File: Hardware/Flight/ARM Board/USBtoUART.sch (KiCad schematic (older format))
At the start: 11 parts

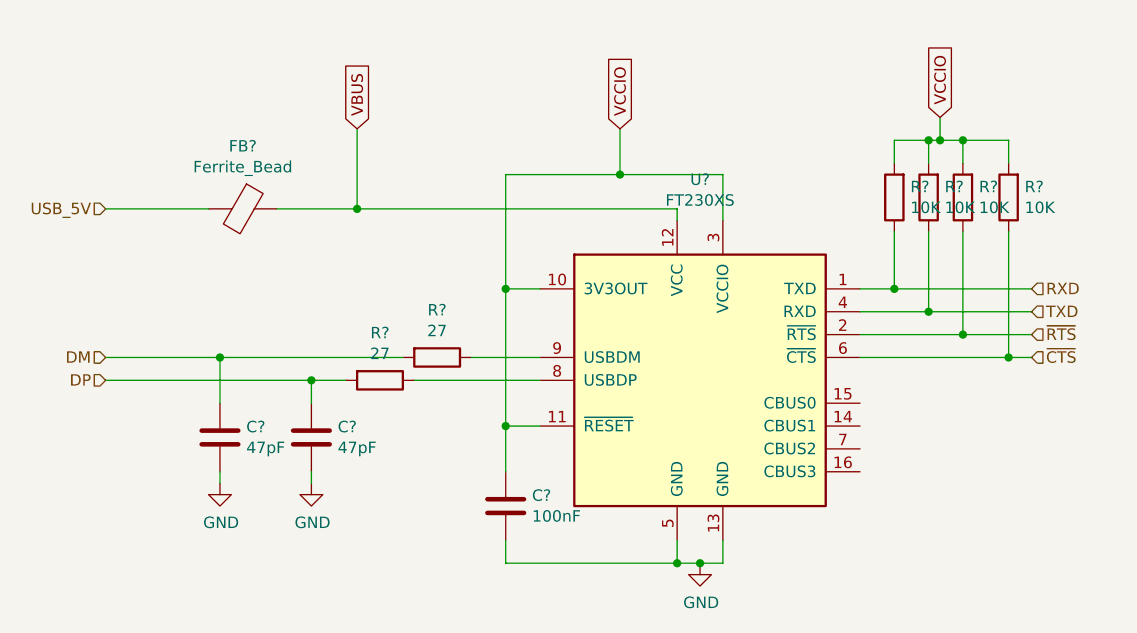
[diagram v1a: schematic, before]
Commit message: Added JTAG I/O, USB UART connections, modified headers and power circuit, added I2C for MSP430
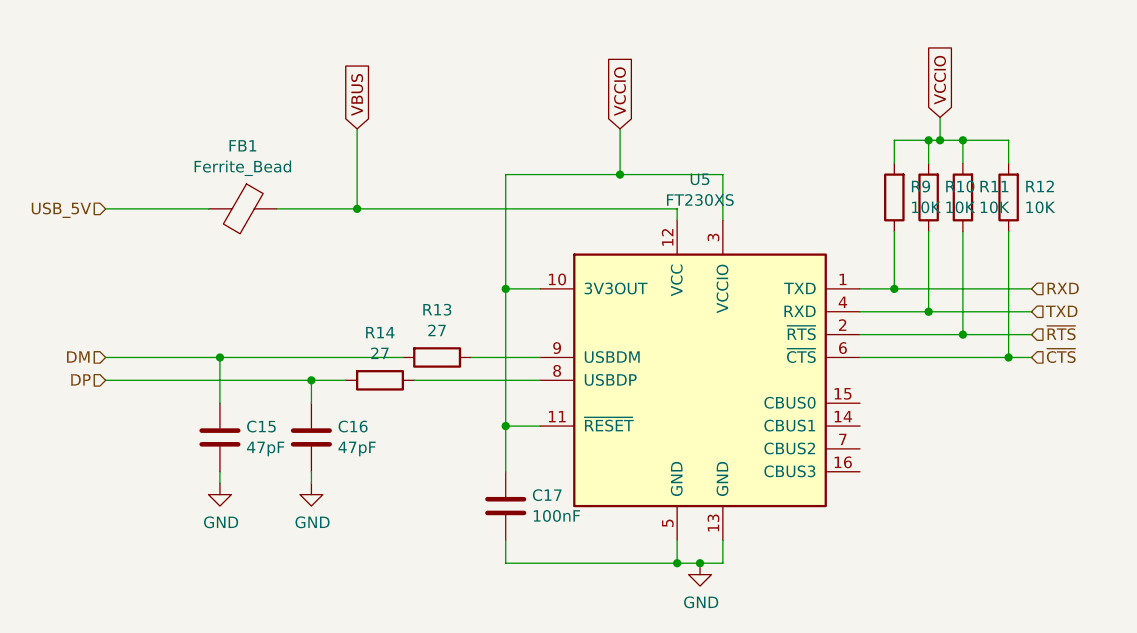
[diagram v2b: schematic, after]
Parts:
- C15, C16: renamed from C?; footprint (none) -> Capacitors_SMD:C_0603
- FB1: renamed from FB?; footprint (none) -> Capacitors_SMD:C_0603
- R10, R11, R12, R13, R14, R9: renamed from R?; footprint (none) -> Resistors_SMD:R_0603
- U5: renamed from U?; footprint Package_SO:SSOP-16_3.9x4.9mm_P0.635mm -> Housings_SSOP:SSOP-16_3.9x4.9mm_Pitch0.635mm
- gave numbers to parts that had none: 1
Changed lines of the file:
@@
 EESchema Schematic File Version 4
+LIBS:ARM Board-cache
 EELAYER 26 0
 EELAYER END
@@
 P 6550 3500
 AR Path="/5C08A0F3" Ref="U?"  Part="1"
-AR Path="/5C089FB0/5C08A0F3" Ref="U?"  Part="1"
-F 0 "U?" H 6550 4378 50  0000 C CNN
+AR Path="/5C089FB0/5C08A0F3" Ref="U5"  Part="1"
+F 0 "U5" H 6550 4378 50  0000 C CNN
 F 1 "FT230XS" H 6550 4287 50  0000 C CNN
-F 2 "Package_SO:SSOP-16_3.9x4.9mm_P0.635mm" H 7000 2850 50  0001 C CNN
+F 2 "Housings_SSOP:SSOP-16_3.9x4.9mm_Pitch0.635mm" H 7000 2850 50  0001 C CNN
 F 3 "http://www.ftdichip.com/Products/ICs/FT230X.html" H 6550 3500 50  0001 C CNN
 	1    6550 3500
@@
 P 4850 3750
 AR Path="/5C08A0FA" Ref="C?"  Part="1"
-AR Path="/5C089FB0/5C08A0FA" Ref="C?"  Part="1"
-F 0 "C?" H 4965 3796 50  0000 L CNN
+AR Path="/5C089FB0/5C08A0FA" Ref="C16"  Part="1"
+F 0 "C16" H 4965 3796 50  0000 L CNN
 F 1 "47pF" H 4965 3705 50  0000 L CNN
-F 2 "" H 4888 3600 50  0001 C CNN
+F 2 "Capacitors_SMD:C_0603" H 4888 3600 50  0001 C CNN
 F 3 "47pF" H 4850 3750 50  0001 C CNN
 	1    4850 3750
@@
 P 4450 3750
 AR Path="/5C08A101" Ref="C?"  Part="1"
-AR Path="/5C089FB0/5C08A101" Ref="C?"  Part="1"
-F 0 "C?" H 4565 3796 50  0000 L CNN
+AR Path="/5C089FB0/5C08A101" Ref="C15"  Part="1"
+F 0 "C15" H 4565 3796 50  0000 L CNN
 F 1 "47pF" H 4565 3705 50  0000 L CNN
-F 2 "" H 4488 3600 50  0001 C CNN
+F 2 "Capacitors_SMD:C_0603" H 4488 3600 50  0001 C CNN
 F 3 "47pF" H 4450 3750 50  0001 C CNN
 	1    4450 3750
@@
 P 5400 3400
 AR Path="/5C08A108" Ref="R?"  Part="1"
-AR Path="/5C089FB0/5C08A108" Ref="R?"  Part="1"
-F 0 "R?" V 5193 3400 50  0000 C CNN
+AR Path="/5C089FB0/5C08A108" Ref="R13"  Part="1"
+F 0 "R13" V 5193 3400 50  0000 C CNN
 F 1 "27" V 5284 3400 50  0000 C CNN
-F 2 "" V 5330 3400 50  0001 C CNN
+F 2 "Resistors_SMD:R_0603" V 5330 3400 50  0001 C CNN
 F 3 "~" H 5400 3400 50  0001 C CNN
 	1    5400 3400
@@
 P 5150 3500
 AR Path="/5C08A10F" Ref="R?"  Part="1"
-AR Path="/5C089FB0/5C08A10F" Ref="R?"  Part="1"
-F 0 "R?" V 4943 3500 50  0000 C CNN
+AR Path="/5C089FB0/5C08A10F" Ref="R14"  Part="1"
+F 0 "R14" V 4943 3500 50  0000 C CNN
 F 1 "27" V 5034 3500 50  0000 C CNN
-F 2 "" V 5080 3500 50  0001 C CNN
+F 2 "Resistors_SMD:R_0603" V 5080 3500 50  0001 C CNN
 F 3 "~" H 5150 3500 50  0001 C CNN
 	1    5150 3500
@@
 P 4550 2750
 AR Path="/5C08A124" Ref="FB?"  Part="1"
-AR Path="/5C089FB0/5C08A124" Ref="FB?"  Part="1"
-F 0 "FB?" V 4276 2750 50  0000 C CNN
+AR Path="/5C089FB0/5C08A124" Ref="FB1"  Part="1"
+F 0 "FB1" V 4276 2750 50  0000 C CNN
 F 1 "Ferrite_Bead" V 4367 2750 50  0000 C CNN
-F 2 "" V 4480 2750 50  0001 C CNN
+F 2 "Capacitors_SMD:C_0603" V 4480 2750 50  0001 C CNN
 F 3 "~" H 4550 2750 50  0001 C CNN
 	1    4550 2750
@@
 P 4450 3950
 AR Path="/5C08A12E" Ref="#PWR?"  Part="1"
-AR Path="/5C089FB0/5C08A12E" Ref="#PWR?"  Part="1"
-F 0 "#PWR?" H 4450 3700 50  0001 C CNN
+AR Path="/5C089FB0/5C08A12E" Ref="#PWR0124"  Part="1"
+F 0 "#PWR0124" H 4450 3700 50  0001 C CNN
 F 1 "GND" H 4455 3777 50  0000 C CNN
 F 2 "" H 4450 3950 50  0001 C CNN
@@
 P 4850 3950
 AR Path="/5C08A134" Ref="#PWR?"  Part="1"
-AR Path="/5C089FB0/5C08A134" Ref="#PWR?"  Part="1"
-F 0 "#PWR?" H 4850 3700 50  0001 C CNN
+AR Path="/5C089FB0/5C08A134" Ref="#PWR0125"  Part="1"
+F 0 "#PWR0125" H 4850 3700 50  0001 C CNN
 F 1 "GND" H 4855 3777 50  0000 C CNN
 F 2 "" H 4850 3950 50  0001 C CNN
@@
 P 6550 4300
 AR Path="/5C08A13C" Ref="#PWR?"  Part="1"
-AR Path="/5C089FB0/5C08A13C" Ref="#PWR?"  Part="1"
-F 0 "#PWR?" H 6550 4050 50  0001 C CNN
+AR Path="/5C089FB0/5C08A13C" Ref="#PWR0126"  Part="1"
+F 0 "#PWR0126" H 6550 4050 50  0001 C CNN
 F 1 "GND" H 6555 4127 50  0000 C CNN
 F 2 "" H 6550 4300 50  0001 C CNN
@@
 P 5700 4050
 AR Path="/5C08A147" Ref="C?"  Part="1"
-AR Path="/5C089FB0/5C08A147" Ref="C?"  Part="1"
-F 0 "C?" H 5815 4096 50  0000 L CNN
+AR Path="/5C089FB0/5C08A147" Ref="C17"  Part="1"
+F 0 "C17" H 5815 4096 50  0000 L CNN
 F 1 "100nF" H 5815 4005 50  0000 L CNN
 F 2 "" H 5738 3900 50  0001 C CNN
@@
 P 7400 2700
 AR Path="/5C08A162" Ref="R?"  Part="1"
-AR Path="/5C089FB0/5C08A162" Ref="R?"  Part="1"
-F 0 "R?" H 7330 2654 50  0000 R CNN
+AR Path="/5C089FB0/5C08A162" Ref="R9"  Part="1"
+F 0 "R9" H 7330 2654 50  0000 R CNN
 F 1 "10K" H 7330 2745 50  0000 R CNN
-F 2 "" V 7330 2700 50  0001 C CNN
+F 2 "Resistors_SMD:R_0603" V 7330 2700 50  0001 C CNN
 F 3 "~" H 7400 2700 50  0001 C CNN
 	1    7400 2700
@@
 P 7550 2700
 AR Path="/5C08A169" Ref="R?"  Part="1"
-AR Path="/5C089FB0/5C08A169" Ref="R?"  Part="1"
-F 0 "R?" H 7480 2654 50  0000 R CNN
+AR Path="/5C089FB0/5C08A169" Ref="R10"  Part="1"
+F 0 "R10" H 7480 2654 50  0000 R CNN
 F 1 "10K" H 7480 2745 50  0000 R CNN
-F 2 "" V 7480 2700 50  0001 C CNN
+F 2 "Resistors_SMD:R_0603" V 7480 2700 50  0001 C CNN
 F 3 "~" H 7550 2700 50  0001 C CNN
 	1    7550 2700
@@
 P 7700 2700
 AR Path="/5C08A170" Ref="R?"  Part="1"
-AR Path="/5C089FB0/5C08A170" Ref="R?"  Part="1"
-F 0 "R?" H 7630 2654 50  0000 R CNN
+AR Path="/5C089FB0/5C08A170" Ref="R11"  Part="1"
+F 0 "R11" H 7630 2654 50  0000 R CNN
 F 1 "10K" H 7630 2745 50  0000 R CNN
-F 2 "" V 7630 2700 50  0001 C CNN
+F 2 "Resistors_SMD:R_0603" V 7630 2700 50  0001 C CNN
 F 3 "~" H 7700 2700 50  0001 C CNN
 	1    7700 2700
@@
 P 7900 2700
 AR Path="/5C08A177" Ref="R?"  Part="1"
-AR Path="/5C089FB0/5C08A177" Ref="R?"  Part="1"
-F 0 "R?" H 7830 2654 50  0000 R CNN
+AR Path="/5C089FB0/5C08A177" Ref="R12"  Part="1"
+F 0 "R12" H 7830 2654 50  0000 R CNN
 F 1 "10K" H 7830 2745 50  0000 R CNN
-F 2 "" V 7830 2700 50  0001 C CNN
+F 2 "Resistors_SMD:R_0603" V 7830 2700 50  0001 C CNN
 F 3 "~" H 7900 2700 50  0001 C CNN
 	1    7900 2700

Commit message: Updated libraries and footprints, netlist
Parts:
- C17: footprint (none) -> Capacitors_SMD:C_0603
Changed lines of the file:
@@
 F 0 "C17" H 5815 4096 50  0000 L CNN
 F 1 "100nF" H 5815 4005 50  0000 L CNN
-F 2 "" H 5738 3900 50  0001 C CNN
+F 2 "Capacitors_SMD:C_0603" H 5738 3900 50  0001 C CNN
 F 3 "47pF" H 5700 4050 50  0001 C CNN
 	1    5700 4050

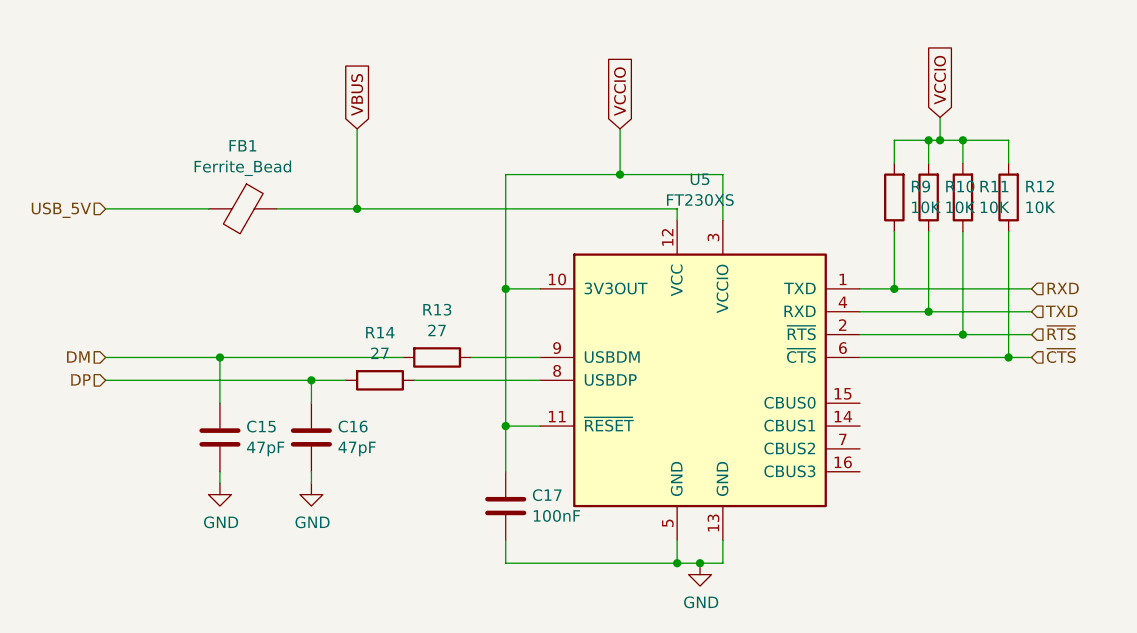
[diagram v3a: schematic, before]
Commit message: SPI added to header, Layout finished
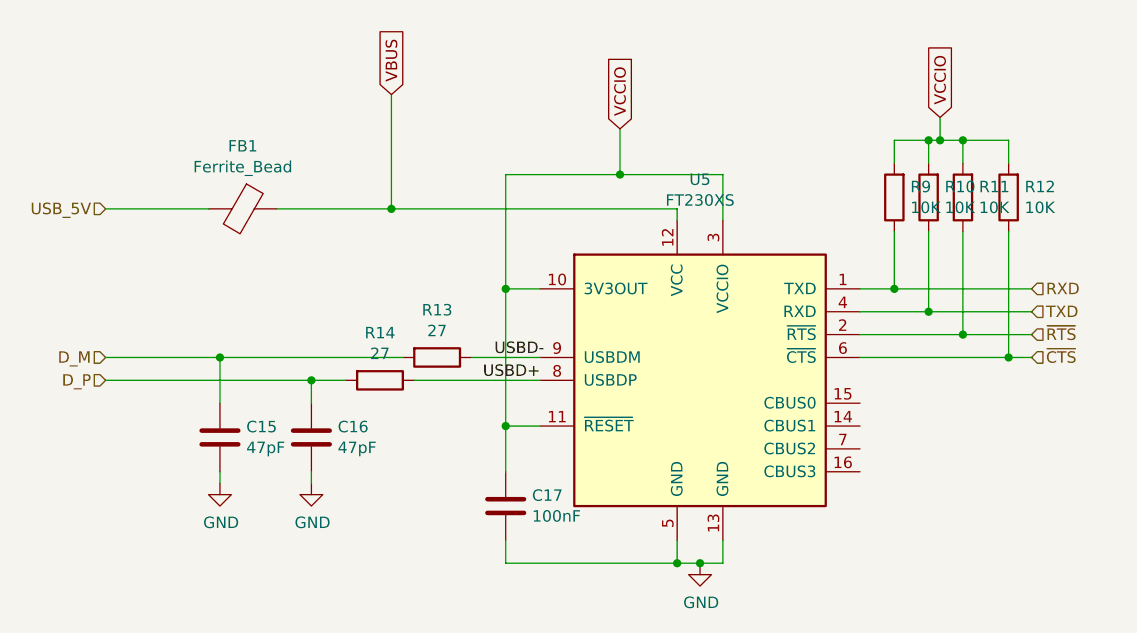
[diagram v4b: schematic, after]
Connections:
- net USBD+: now reaches R14.1, U5.8 (USBDP)
- net USBD-: now reaches R13.1, U5.9 (USBDM)
- net DM renamed D_M
- net DP renamed D_P
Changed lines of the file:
@@
 Wire Wire Line
 	4850 3500 4850 3600
-Text GLabel 5050 2400 1    50   Input ~ 0
-VBUS
 Connection ~ 4850 3500
 $Comp
@@
 Wire Wire Line
 	3950 2750 4400 2750
-Wire Wire Line
-	4700 2750 5050 2750
-Wire Wire Line
-	5050 2750 5050 2400
 $Comp
 L power:GND #PWR?
@@
 Connection ~ 5700 3100
 Wire Wire Line
-	5050 2750 6450 2750
-Wire Wire Line
 	6450 2750 6450 2800
-Connection ~ 5050 2750
 Text GLabel 6200 2400 1    50   Input ~ 0
 VCCIO
@@
 USB_5V
 Text HLabel 3950 3400 0    50   Input ~ 0
-DM
+D_M
 Text HLabel 3950 3500 0    50   Input ~ 0
-DP
+D_P
 Wire Wire Line
 	3950 3500 4850 3500
@@
 	3950 3400 4450 3400
 Connection ~ 4450 3400
+Wire Wire Line
+	4700 2750 5200 2750
+Text GLabel 5200 2250 1    50   Input ~ 0
+VBUS
+Wire Wire Line
+	5200 2250 5200 2750
+Connection ~ 5200 2750
+Wire Wire Line
+	5200 2750 6450 2750
+Text Label 5650 3400 0    50   ~ 0
+USBD-
+Text Label 5600 3500 0    50   ~ 0
+USBD+
 $EndSCHEMATC

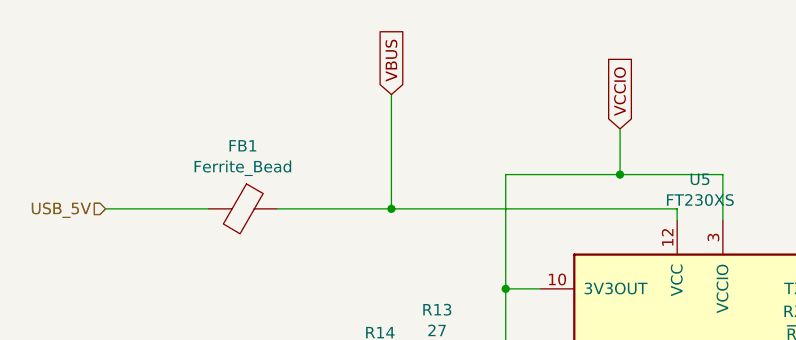
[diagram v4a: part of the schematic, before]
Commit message: ARM board refactor
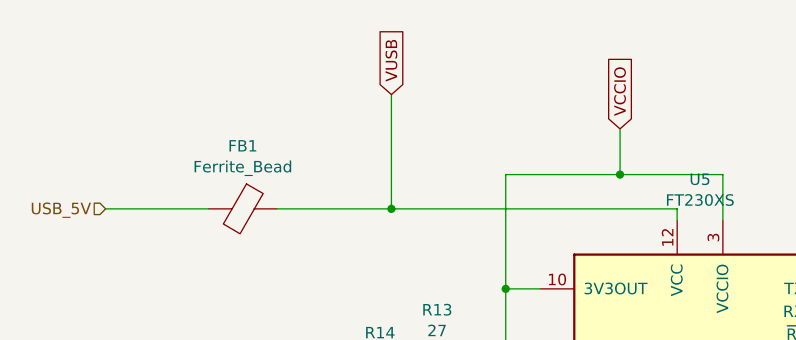
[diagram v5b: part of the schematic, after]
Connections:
- net VBUS renamed VUSB
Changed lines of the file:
@@
 $Descr A4 11693 8268
 encoding utf-8
-Sheet 2 2
+Sheet 2 4
 Title ""
 Date ""
@@
 	4700 2750 5200 2750
 Text GLabel 5200 2250 1    50   Input ~ 0
-VBUS
+VUSB
 Wire Wire Line
 	5200 2250 5200 2750
